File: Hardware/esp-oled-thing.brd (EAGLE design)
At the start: 48.3 x 27 mm, 44 parts, among them Q1 2.5A/30V, U1 MCP73831, U2 TPS61200

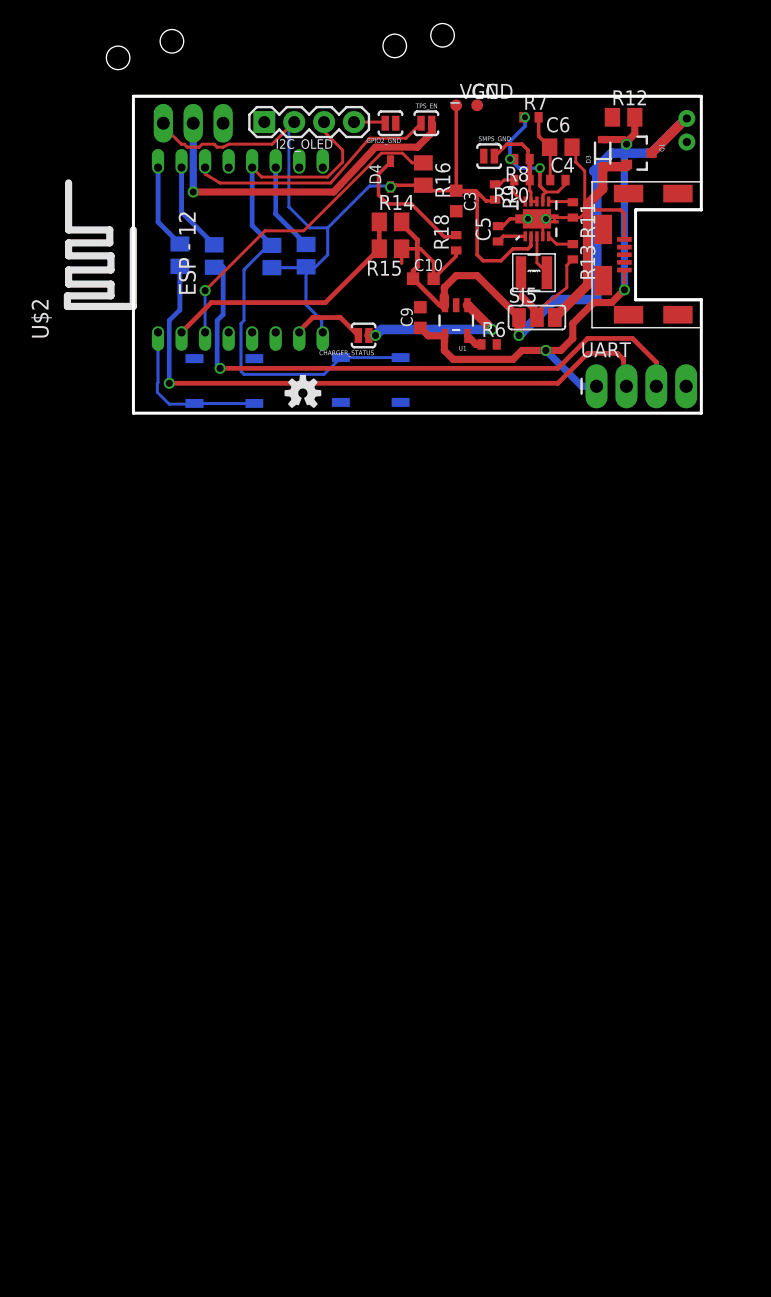
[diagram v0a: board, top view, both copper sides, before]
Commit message: layout and components modified for better solderability.
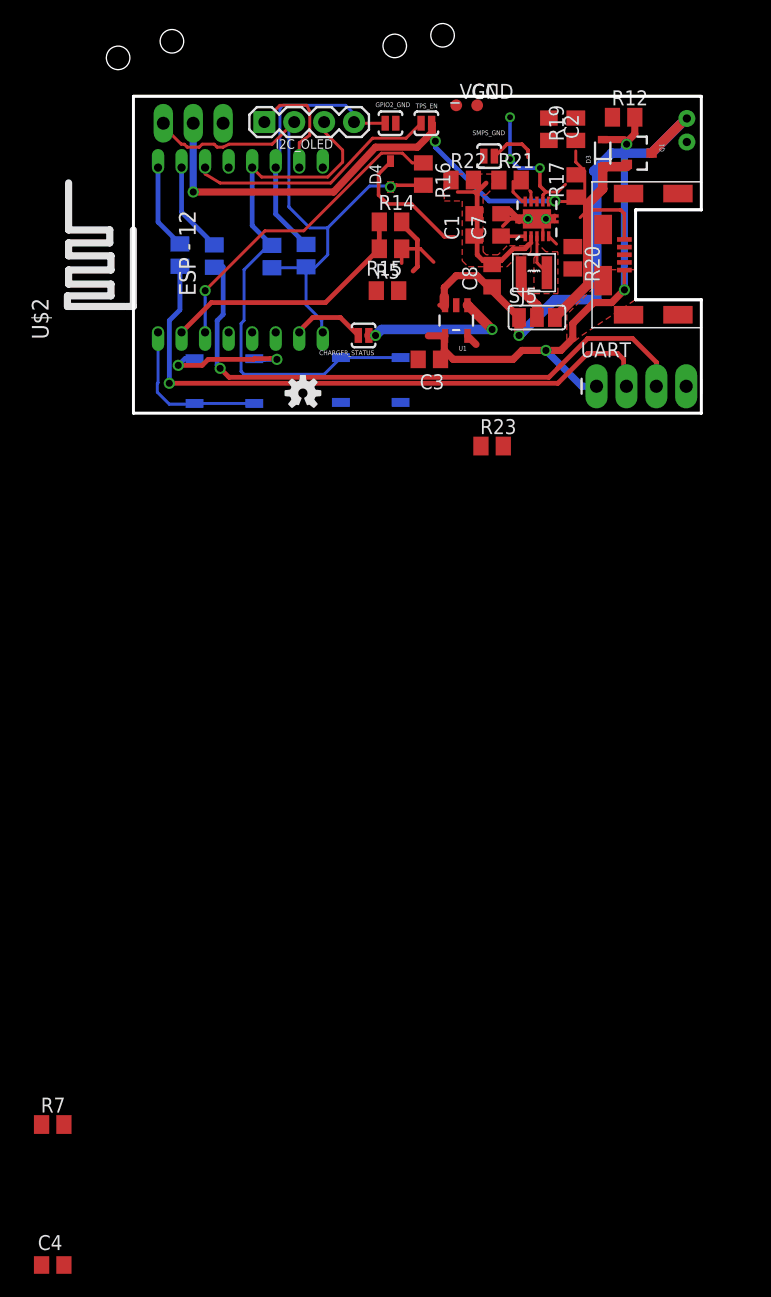
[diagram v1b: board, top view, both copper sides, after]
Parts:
- removed C10, C9: 4.7uF, rcl:C0603K
- removed C5: 0.1uF, rcl:C0402
- removed C6: 10uF, rcl:C0805
- removed R10, R8: 220k, rcl:R0402
- removed R11: 10k, rcl:R0402
- removed R13: 100E, rcl:R0402
- removed R18: 470E, rcl:R0402
- removed R6: 2k, rcl:R0402
- removed R9: 1.2M, rcl:R0402
- added C1: 10uF, rcl:C0805
- added C2, C7: 0.1uF, rcl:C0805
- added C8: 22uF, rcl:C0805
- added R17, R21: 220K, adafruit:M0805
- added R19: 2M, adafruit:M0805
- added R20: 100E, adafruit:M0805
- added R22: 1.2M, adafruit:M0805
- added R23: 470E, adafruit:M0805
- added R5: 10K, adafruit:M0805
- C3: value 22uF -> 4.7uF; device rcl:C0603K -> rcl:C0805
- C4: value 0.1uF -> 4.7uF; device rcl:C0402 -> rcl:C0805
- GPIO2_GND, TPS_EN: value SOLDERJUMPERNO -> (none)
- R7: value 2M -> 2K; device rcl:R0402 -> adafruit:M0805
- moved C4 101.7 mm to (-6.86, -72.4)
- moved R7 94.8 mm to (-6.86, -60.5)
- moved C3 13.7 mm to (25.1, 4.57), turned to 180 degrees
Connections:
- net 5VIN: now also C3.1; no longer C9.1
- net FB: now also R21.2, R22.1; no longer R10.2, R9.1
- net GND: now also C1.2, C4.2, C7.2, C8.2, R23.1, R5.1, R7.1; no longer C10.2, C5.2, C6.2, C9.2, R11.2, R18.1, R6.2
- net GND1: now also R17.1, R21.1; no longer R10.1, R8.1
- net N$13: now also R7.2; no longer R6.1
- net N$18: now also C7.1; no longer C5.1
- net N$21: now also R23.2; no longer R18.2
- net SYSPOWER_IN: now also C1.1, C2.1, R19.2, R20.2; no longer C4.1, C6.1, R13.2, R7.2
- net TPS_EN: now also R5.2; no longer R11.1
- net UVLO: now also C2.2, R17.2, R19.1; no longer C4.2, R7.1, R8.2
- net VBATT: now also C4.1; no longer C10.1
- net VCC: now also C8.1, R22.2; no longer C3.1, R9.2
- net VIN: now also R20.1; no longer R13.1
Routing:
- net GND: track 30.5 -> 48.1 mm, vias 2 -> 4
- net SYSPOWER_IN: track 20.9 -> 4.88 mm
- net TPS_EN: track 31.2 -> 45.1 mm, vias 1 -> 3
- net SDA: track 10.4 -> 23.0 mm
- net VCC: track 76.1 -> 63.8 mm
- net VBATT: track 54.0 -> 50.2 mm
- net GND1: track 8.46 -> 5.58 mm
- net FB: track 4.22 -> 2.27 mm
- net VIN: track 2.33 -> 0.95 mm
- net UVLO: track 12.5 -> 11.5 mm
- net N$18: track 2.82 -> 1.86 mm
- net 5VIN: track 46.9 -> 45.9 mm
- net N$8: track 50.7 -> 51.4 mm
- added copper zone on layer 1, net 5VIN
- added copper zone on layer 1, net N$14
- added copper zone on layer 1, net VCC

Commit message: Preliminary layout finished. Replaced passives with easier to solder 0805 parts. needs more optimization
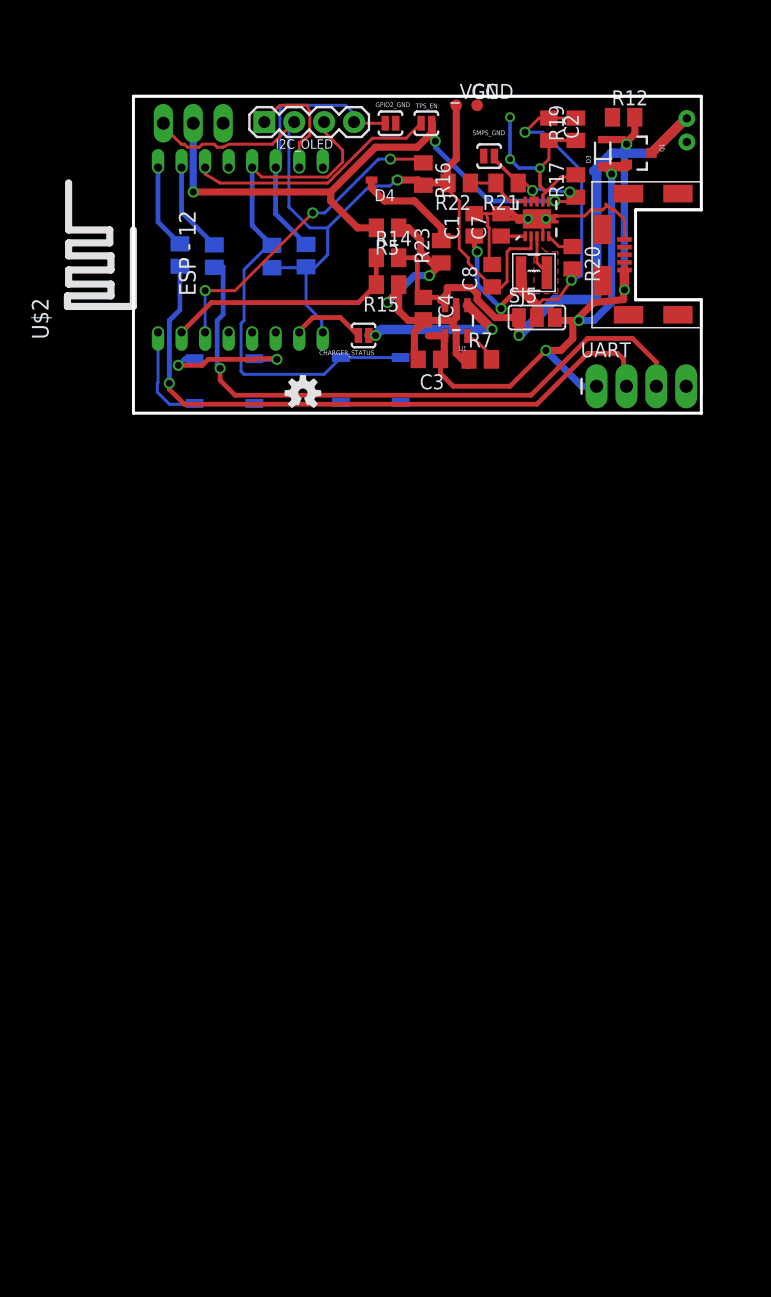
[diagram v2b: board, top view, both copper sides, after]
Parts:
- moved C4 87.2 mm to (24.6, 8.89), turned to 270 degrees
- moved R7 74.5 mm to (29.5, 4.57)
- moved R23 17.1 mm to (26.2, 13.7), turned to 90 degrees
- moved R5 5.33 mm to (21.6, 15.7), turned to 180 degrees
- moved R14 3.06 mm to (21.6, 13.2)
- moved R15 3.06 mm to (21.6, 10.9)
- moved D4 0.72 mm to (21.3, 19.8), turned to 180 degrees
- moved R22 0.36 mm to (27.7, 19.6), turned to 180 degrees
- moved R21 0.36 mm to (31.8, 19.6), turned to 180 degrees
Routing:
- net SYSPOWER_IN: track 4.88 -> 41.7 mm, vias 0 -> 4
- net GND: track 48.1 -> 76.8 mm, vias 4 -> 6
- net VCC: track 63.8 -> 75.8 mm
- net UVLO: track 11.5 -> 17.7 mm
- net TPS_EN: track 45.1 -> 50.6 mm
- net GND1: track 5.58 -> 10.5 mm, vias 0 -> 2
- net 5VIN: track 45.9 -> 49.8 mm
- net FB: track 2.27 -> 5.71 mm
- net POWERPATH_OUT: track 16.8 -> 19.8 mm, vias 0 -> 2
- net N$13: track 1.04 -> 2.99 mm
- net N$8: track 51.4 -> 53.2 mm
- net N$4: track 52.6 -> 54.3 mm
- net N$2: track 22.0 -> 20.5 mm
- net VIN: track 0.95 -> 2.41 mm
- net N$21: track 11.2 -> 10.4 mm
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- removed copper zone on layer 1, net 5VIN
- removed copper zone on layer 1, net VCC

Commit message: drc and cleanup in progress
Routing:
- net VCC: track 75.8 -> 85.2 mm
- net N$6: track 0.00 -> 5.33 mm
- net SYSPOWER_IN: track 41.7 -> 46.7 mm
- net N$22: track 0.00 -> 2.54 mm
- net N$9: track 0.00 -> 2.41 mm
- net GND1: track 10.5 -> 12.3 mm
- net N$10: track 0.00 -> 1.78 mm
- net FB: track 5.71 -> 7.49 mm
- net GND: track 76.8 -> 78.4 mm
- net TPS_EN: track 50.6 -> 49.0 mm
- net N$16: track 0.00 -> 1.52 mm
- net N$15: track 0.00 -> 1.52 mm
- net N$17: track 0.00 -> 1.27 mm
- net N$12: track 0.00 -> 1.27 mm
- net N$11: track 0.00 -> 1.27 mm
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
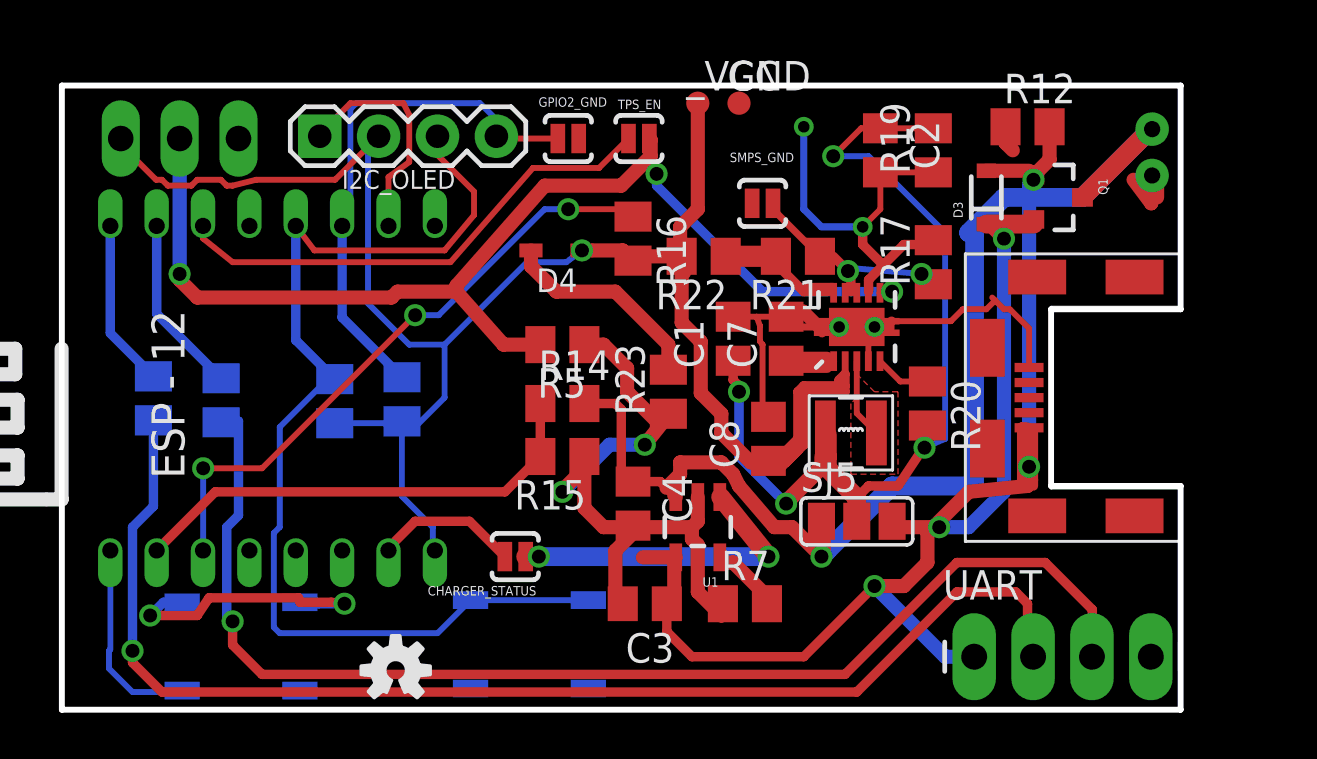
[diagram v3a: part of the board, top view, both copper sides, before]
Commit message: routing done. need to clean up the silkscreen. first commit from new lab (apartment?)
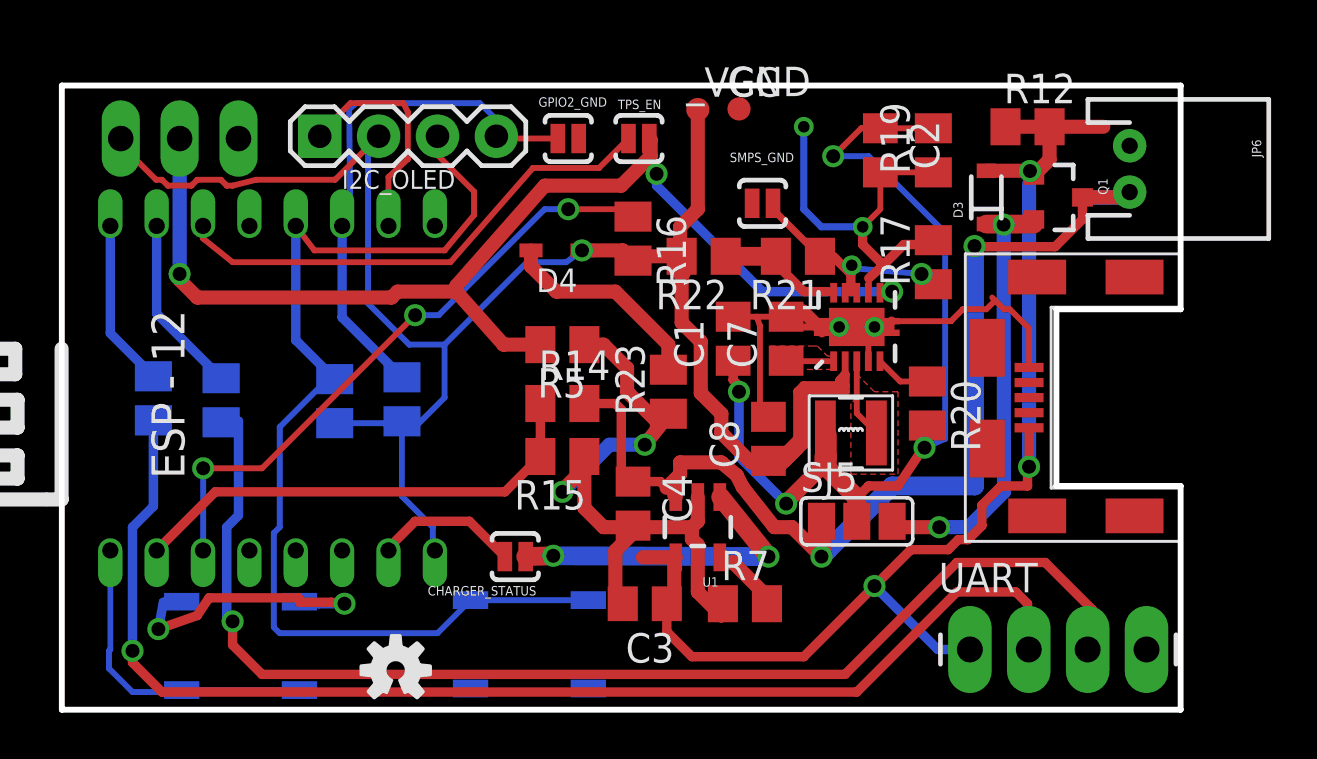
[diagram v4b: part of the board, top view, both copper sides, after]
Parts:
- moved JP6 1.21 mm to (46.1, 23.3), flipped to the top, turned to 270 degrees
- moved UART 0.36 mm to (39.2, 2.60)
- moved _VCC 0.27 mm to (27.4, 25.9)
- moved GND 0.25 mm to (29.2, 25.9)
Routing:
- net N$6: track 5.33 -> 0.00 mm
- net VBATT: track 51.5 -> 47.0 mm, vias 1 -> 2
- net GND: track 78.4 -> 81.8 mm
- net N$22: track 2.54 -> 0.00 mm
- net N$10: track 1.78 -> 0.00 mm
- net FB: track 7.49 -> 5.90 mm
- net N$16: track 1.52 -> 0.00 mm
- net N$15: track 1.52 -> 0.00 mm
- net N$17: track 1.27 -> 0.00 mm
- net N$12: track 1.27 -> 0.00 mm
- net N$11: track 1.27 -> 0.00 mm
- net N$23: track 1.02 -> 0.00 mm
- net GND1: track 12.3 -> 11.6 mm
- net 5VIN: track 49.8 -> 49.7 mm, vias 4 -> 3
- added copper zone on layer 1, net N$18
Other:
- outline, holes or cut-outs redrawn

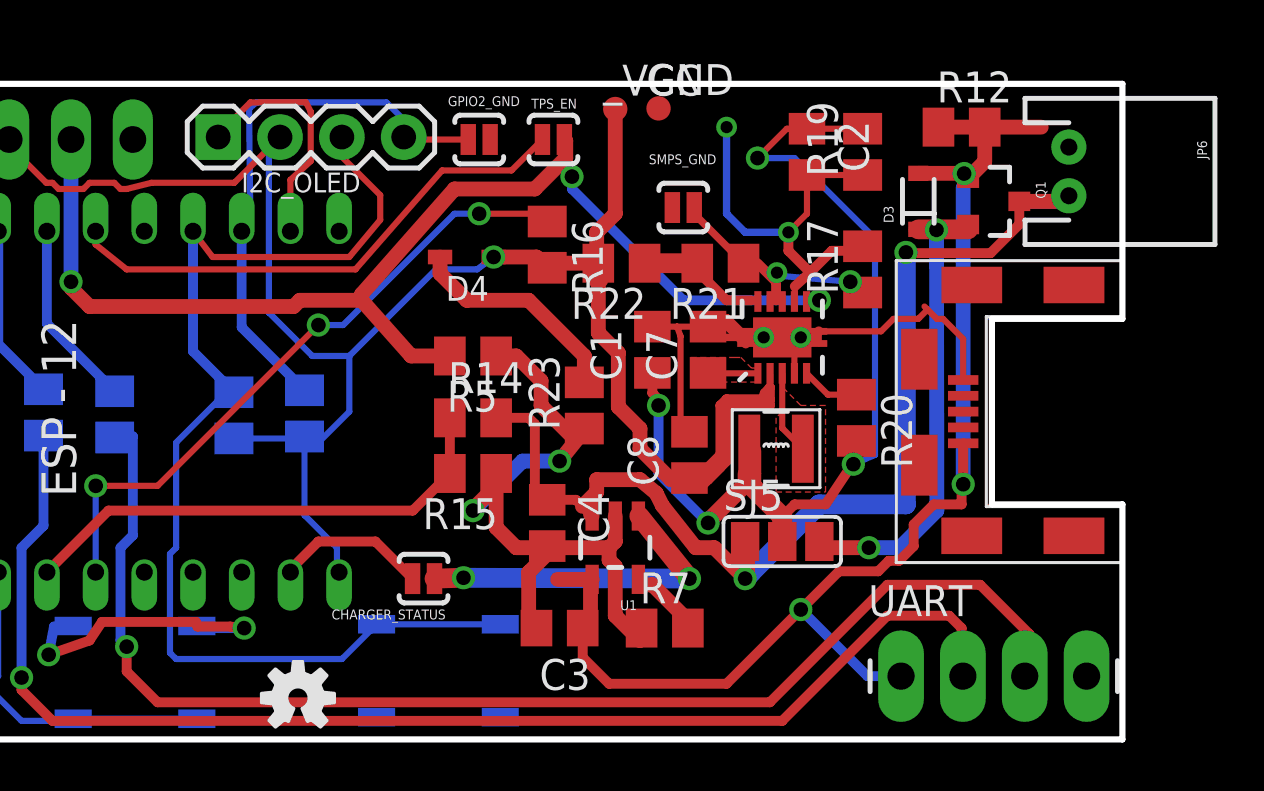
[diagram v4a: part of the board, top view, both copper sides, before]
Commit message: silkscreen fixed, minor issues pending, will attempt to optimize the layout further.
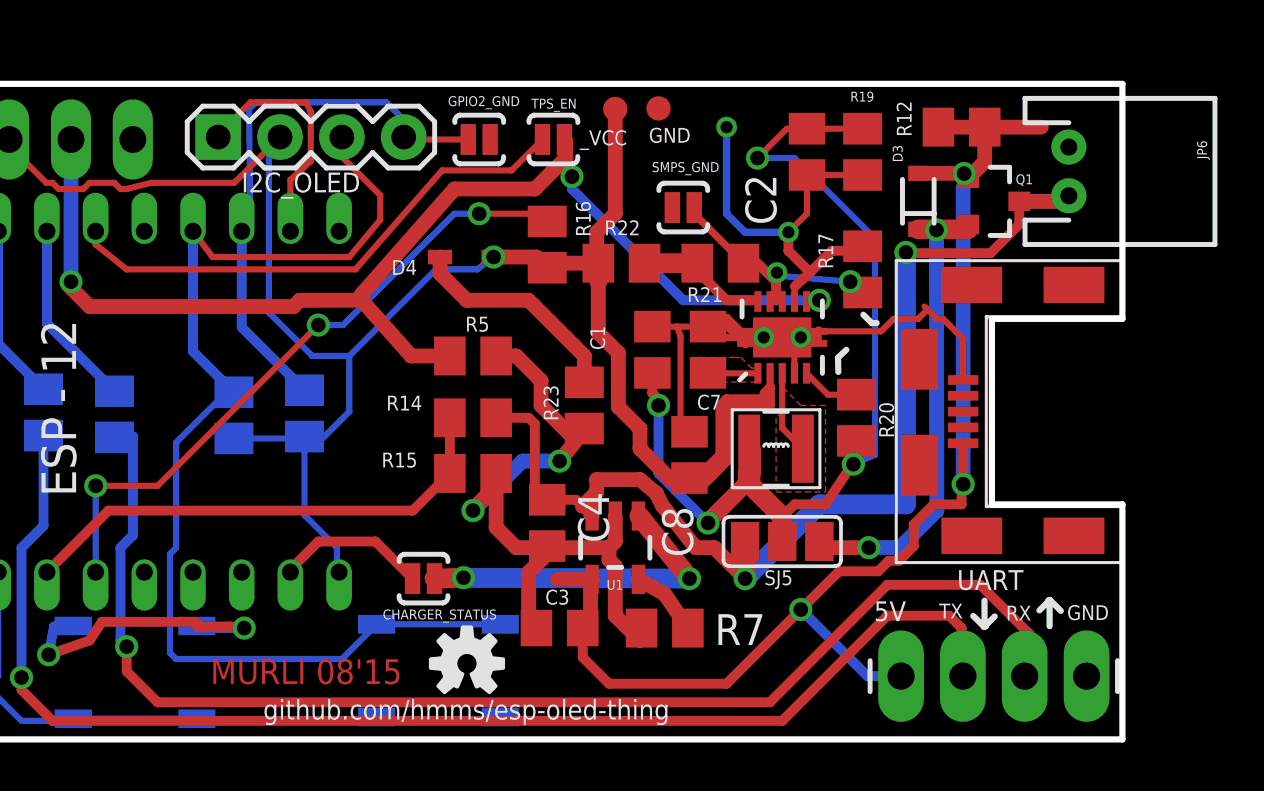
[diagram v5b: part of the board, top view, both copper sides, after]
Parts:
- moved U$1 7.08 mm to (21.3, 3.11)
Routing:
- net N$9: track 2.41 -> 0.00 mm
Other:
- board text added: "5V"
- board text added: "GND"
- board text added: "MURLI 08'15"
- board text added: "RX"
- board text added: "TX"
- board text added: "github.com/hmms/esp-oled-thing"
